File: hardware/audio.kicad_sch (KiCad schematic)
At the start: 0 parts

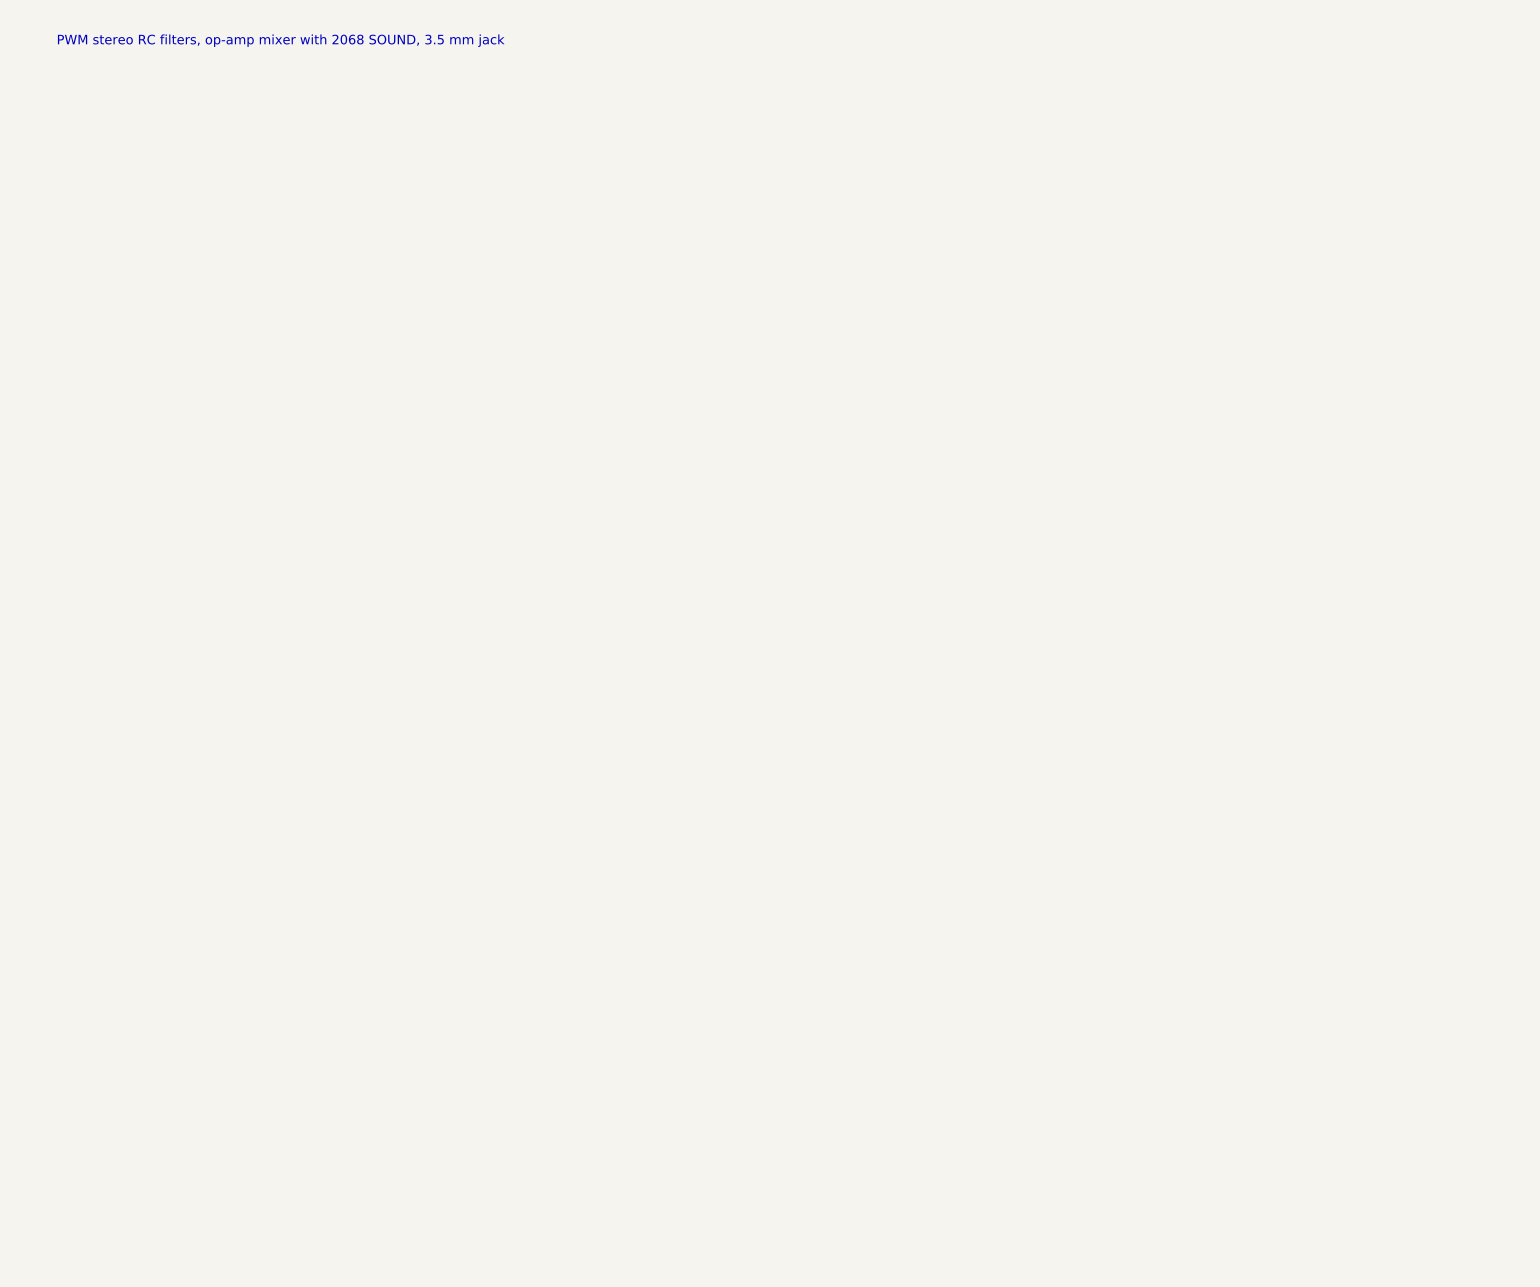
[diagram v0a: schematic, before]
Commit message: Remaining sheets: power, SD and display, WiFi, audio, joystick; ERC clean
- Power: Schottky diode-OR of edge +5V and USB VBUS (card runs from the
  2068/expansion bus, USB alone, or both), two TLV1117LV33 LDOs, bulk caps
- SD: Hirose DM3AT in SPI mode with series R, pull-ups, card detect to STAT
- OLED: 7-pin header (Waveshare 1.27in 128x96 SSD1351) on SPI1
- WiFi: ESP32-C3-WROOM-02 on UART, EN/boot from CTL, IO8 pull-up
- Audio: PWM low-pass, 2068 SOUND mix, MCP6002 buffers, 3.5 mm jack
- Joystick: DE-9 Kempston with pull-ups, series R, optional +5V jumper
- Memory sheet: activity LED on CTL bit 6
- Docs: power decision updated

Co-Authored-By: Claude Fable 5.1 <noreply@anthropic.com>
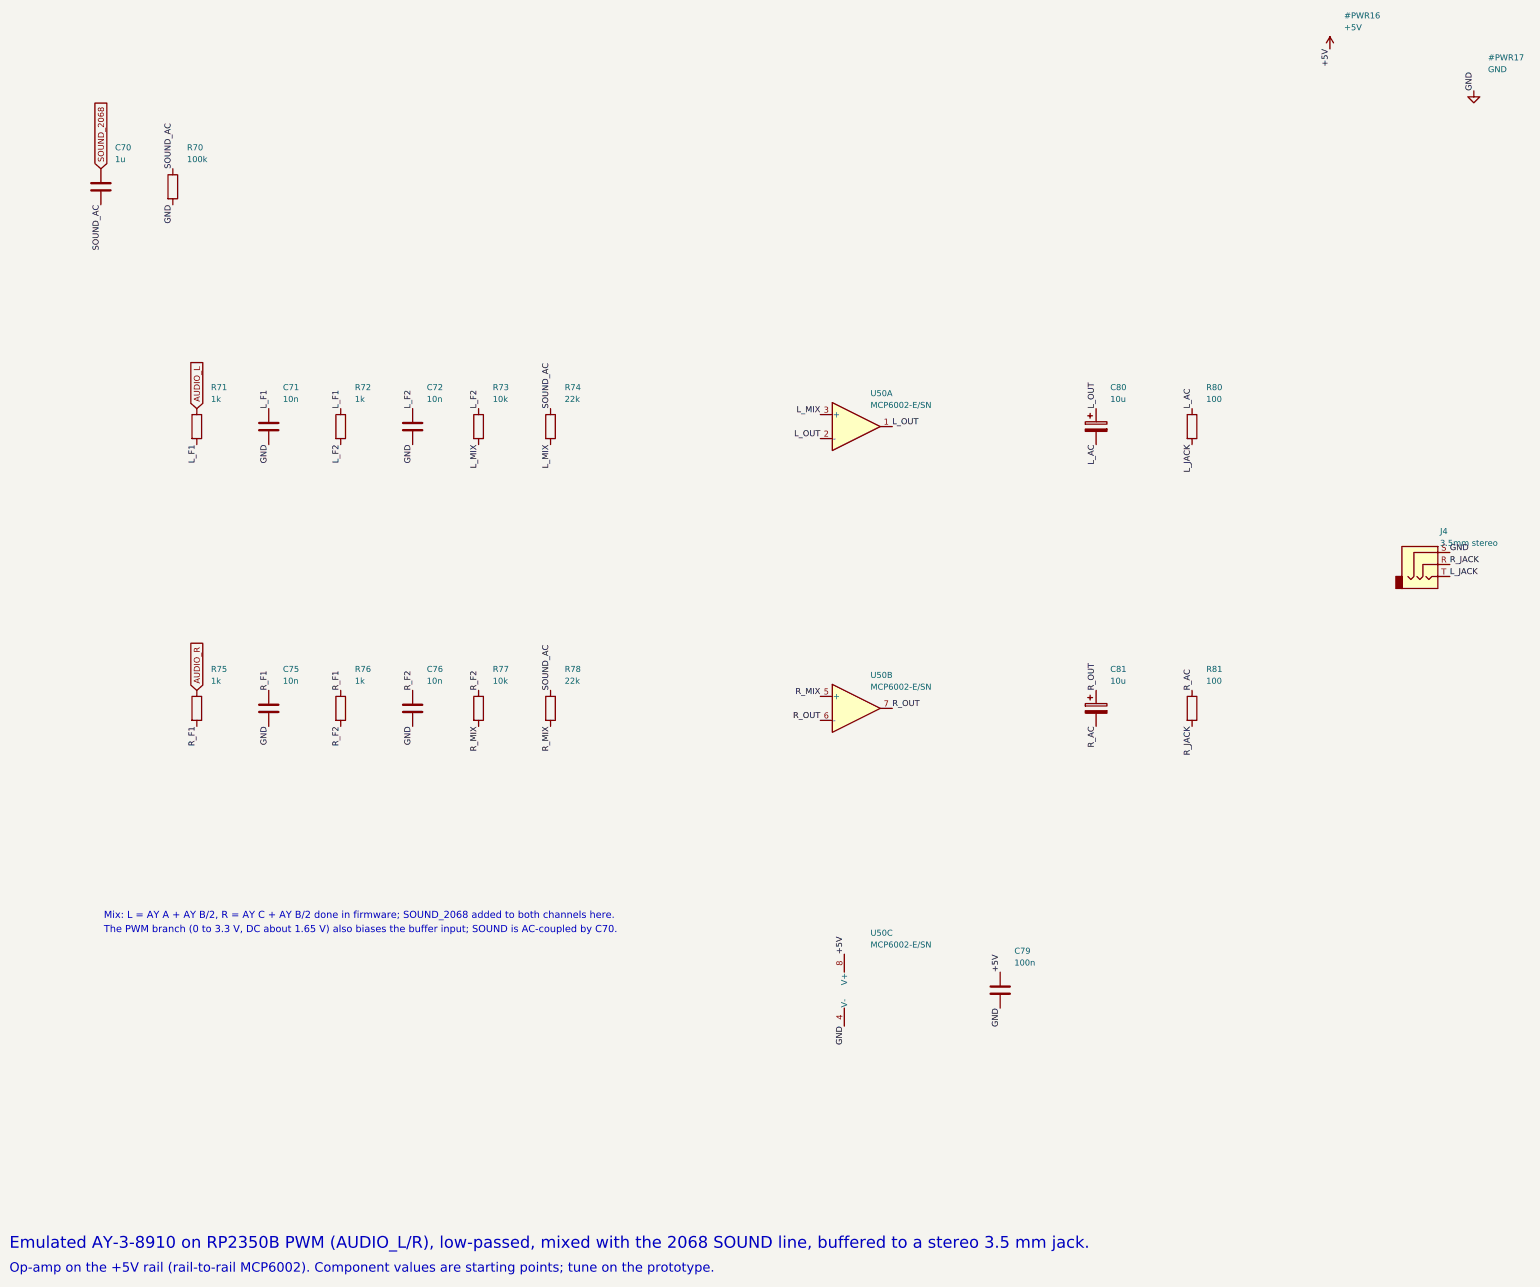
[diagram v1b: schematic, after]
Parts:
- added C70: 1u, Capacitor_SMD:C_0603_1608Metric, symbol Device:C
- added C71, C72, C75, C76: 10n, Capacitor_SMD:C_0603_1608Metric, symbol Device:C
- added C79: 100n, Capacitor_SMD:C_0603_1608Metric, symbol Device:C
- added C80, C81: 10u, Capacitor_SMD:C_0805_2012Metric, symbol Device:C_Polarized
- added J4: 3.5mm stereo, Connector_Audio:Jack_3.5mm_CUI_SJ-3523-SMT_Horizontal, symbol Connector_Audio:AudioJack3
- added R70: 100k, Resistor_SMD:R_0603_1608Metric, symbol Device:R
- added R71, R72, R75, R76: 1k, Resistor_SMD:R_0603_1608Metric, symbol Device:R
- added R73, R77: 10k, Resistor_SMD:R_0603_1608Metric, symbol Device:R
- added R74, R78: 22k, Resistor_SMD:R_0603_1608Metric, symbol Device:R
- added R80, R81: 100, Resistor_SMD:R_0603_1608Metric, symbol Device:R
- added U50: MCP6002-E/SN, Package_SO:SOIC-8_3.9x4.9mm_P1.27mm, symbol Amplifier_Operational:MCP6002-xSN
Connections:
- new net +5V: C79.1, U50.8 (V+)
- new net AUDIO_L: R71.1
- new net AUDIO_R: R75.1
- new net GND: C71.2, C72.2, C75.2, C76.2, C79.2, J4.S, R70.2, U50.4 (V-)
- new net L_AC: C80.2, R80.1
- new net L_F1: C71.1, R71.2, R72.1
- new net L_F2: C72.1, R72.2, R73.1
- new net L_JACK: J4.T, R80.2
- new net L_MIX: R73.2, R74.2, U50.3 (+)
- new net L_OUT: C80.1, U50.1, U50.2 (-)
- new net R_AC: C81.2, R81.1
- new net R_F1: C75.1, R75.2, R76.1
- new net R_F2: C76.1, R76.2, R77.1
- new net R_JACK: J4.R, R81.2
- new net R_MIX: R77.2, R78.2, U50.5 (+)
- new net R_OUT: C81.1, U50.6 (-), U50.7
- new net SOUND_2068: C70.1
- new net SOUND_AC: C70.2, R70.1, R74.1, R78.1
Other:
- note added: "Emulated AY-3-8910 on RP2350B PWM (AUDIO_L/R), low-passed, mixed with the 2068 SOUND line, buffered to a stereo 3.5 mm jack."
- note added: "Mix: L = AY A + AY B/2, R = AY C + AY B/2 done in firmware; SOUND_2068 added to both channels here."
- note added: "Op-amp on the +5V rail (rail-to-rail MCP6002). Component values are starting points; tune on the prototype."
- note added: "The PWM branch (0 to 3.3 V, DC about 1.65 V) also biases the buffer input; SOUND is AC-coupled by C70."
- note removed: "PWM stereo RC filters, op-amp mixer with 2068 SOUND, 3.5 mm jack"

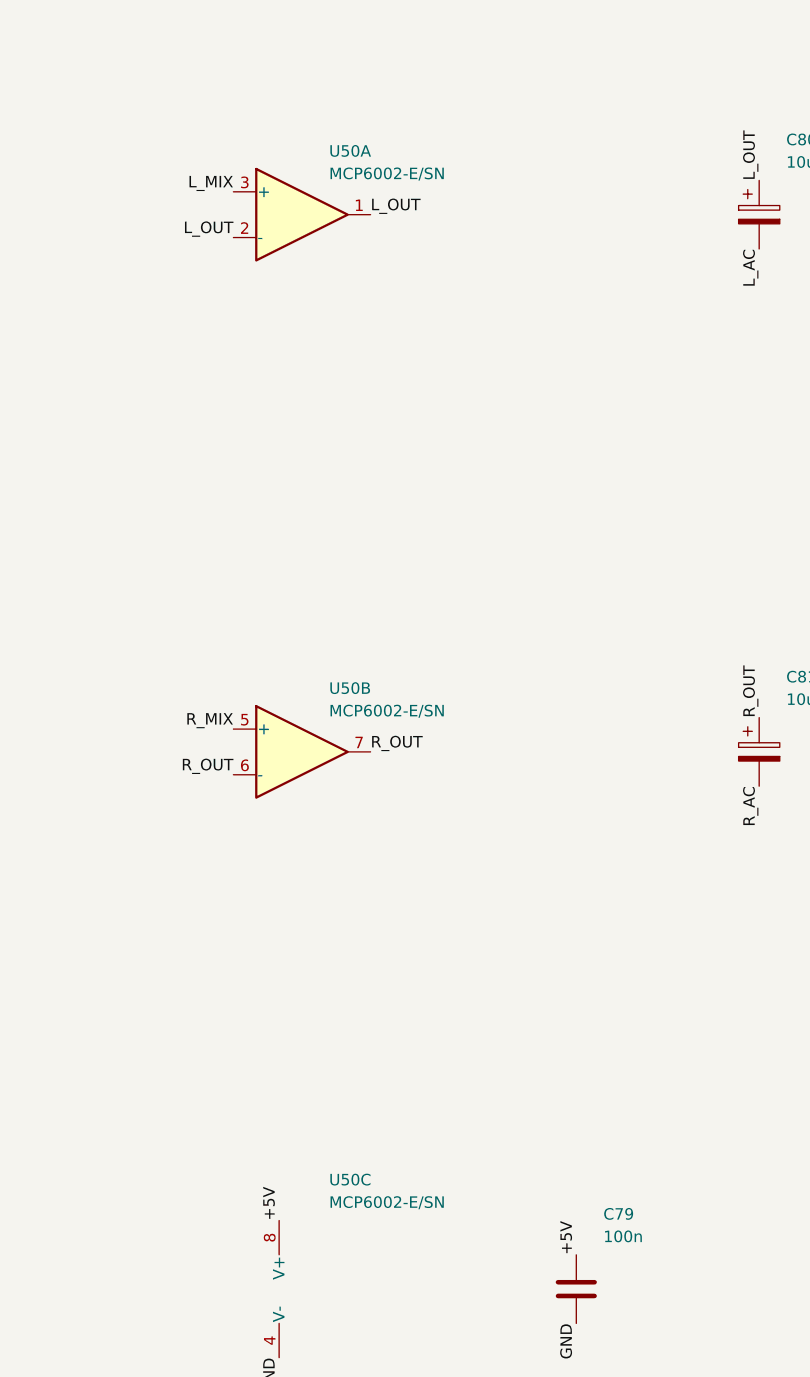
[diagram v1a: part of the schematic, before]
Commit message: BOM pass: LCSC and MPN fields on every part, JLCPCB BOM export
- scripts/parts.py: part table looked up 2026-09-16; schlib stamps fields
- substitutions for stock: 74HC273PW, 74LVC139PW, TI LVC04/08/126/574/1G86,
  33R USB series, XKB TS-1187A switches, Panasonic polymer 220uF, B5819W
- bom/: JLCPCB-format and full BOM CSVs

Co-Authored-By: Claude Fable 5.1 <noreply@anthropic.com>
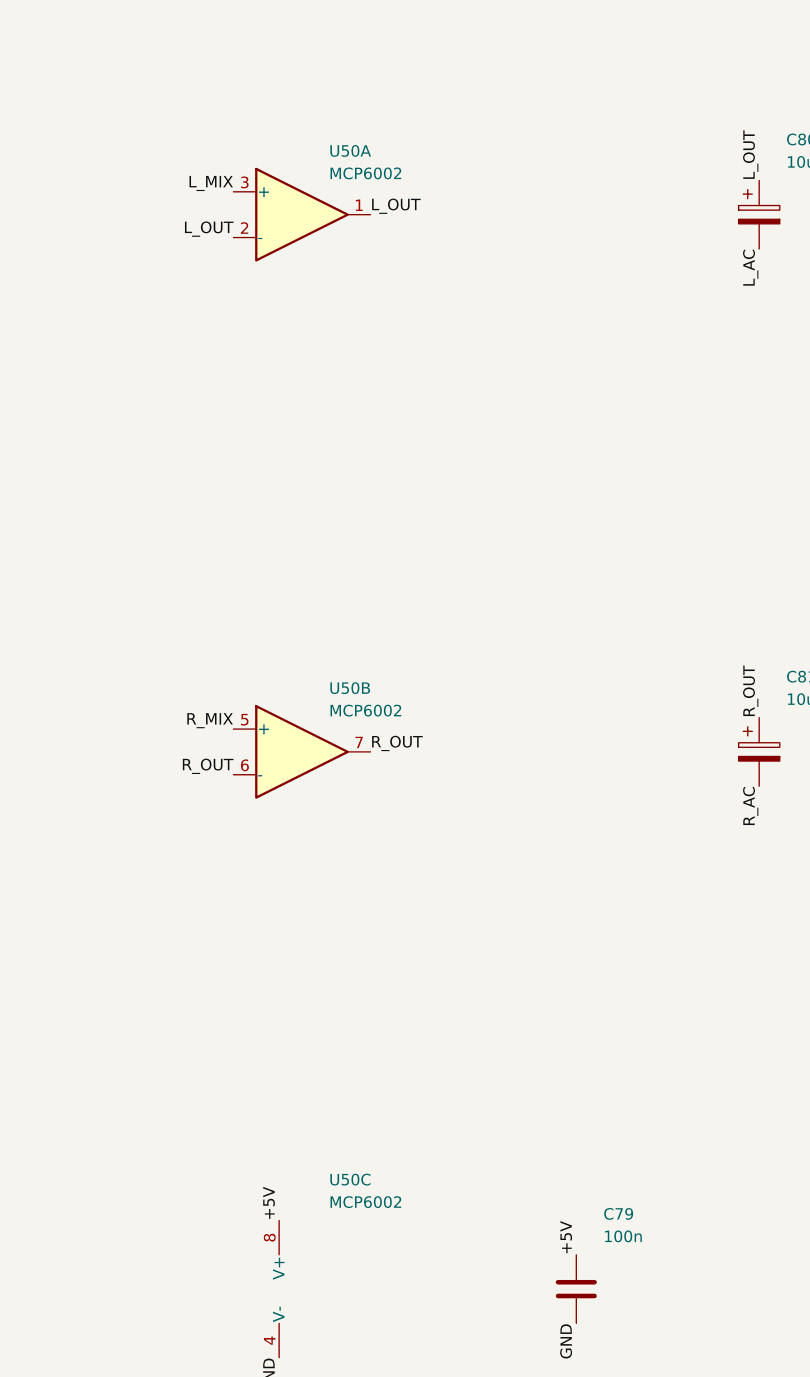
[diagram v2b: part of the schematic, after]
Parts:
- C70: LCSC (none) -> C15849; MPN (none) -> CL10A105KB8NNNC
- C71, C72, C75, C76: LCSC (none) -> C57112; MPN (none) -> CL10B103KB8NNNC
- C79: LCSC (none) -> C14663; MPN (none) -> CC0603KRX7R9BB104
- C80, C81: LCSC (none) -> C15850; MPN (none) -> CL21A106KAYNNNE
- J4: LCSC (none) -> C4991872; MPN (none) -> SJ-3523-SMT-TR
- R70: LCSC (none) -> C25803; MPN (none) -> 0603WAF1003T5E
- R71, R72, R75, R76: LCSC (none) -> C21190; MPN (none) -> 0603WAF1001T5E
- R73, R77: LCSC (none) -> C25804; MPN (none) -> 0603WAF1002T5E
- R74, R78: LCSC (none) -> C31850; MPN (none) -> 0603WAF2202T5E
- R80, R81: LCSC (none) -> C22775; MPN (none) -> 0603WAF1000T5E
- U50: value MCP6002-E/SN -> MCP6002; LCSC (none) -> C125816; MPN (none) -> MCP6002T-E/SN
